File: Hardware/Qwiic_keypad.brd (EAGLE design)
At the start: 25.4 x 25.4 mm, 36 parts, among them J3 PTH, J6 AVR_SPI_PROG_3X2TESTPOINTS, U3 ATTINY84

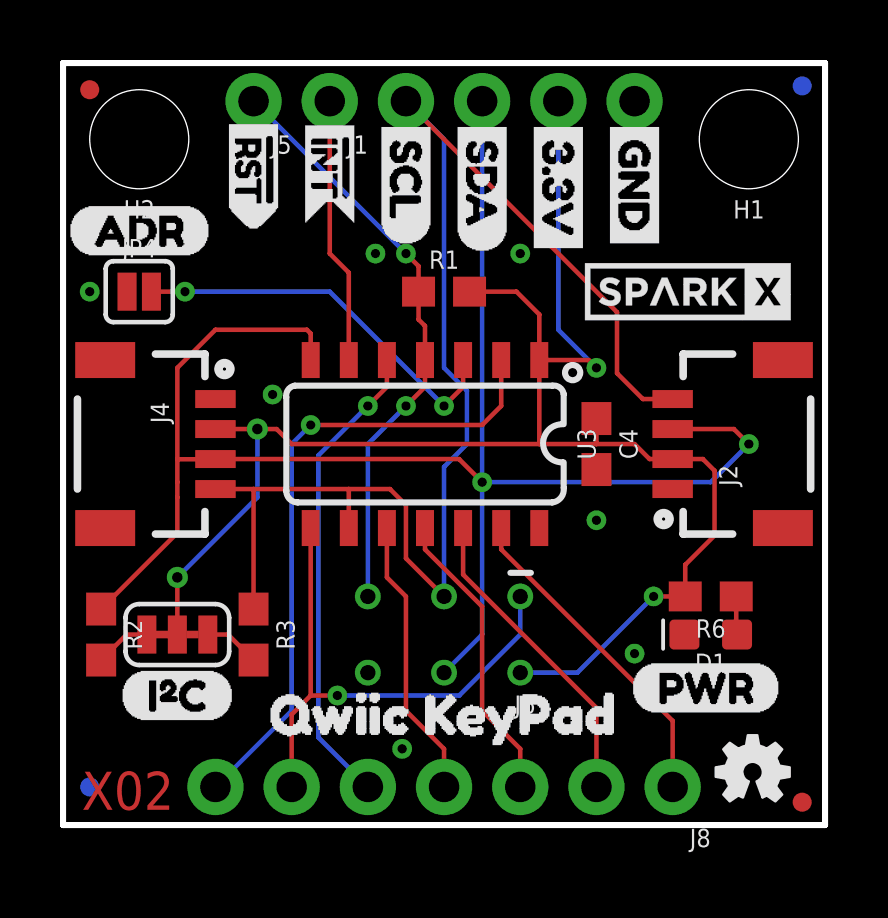
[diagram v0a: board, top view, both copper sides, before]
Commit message: updating hardware
-SFE logo in schematic (w/ slight re-arrange to fit)

-changed version in sch (and brd) to v10

-bumped traces up from 6 mils to 8 mils.

-bumped vias up from 12 mils to 15 mils.

-switched to "sfe tight" drc

-minor trace nudgeing to avoid clearance warnings.

-increased "pass through" 3.3V trace to 16 mils. added more GND vias.
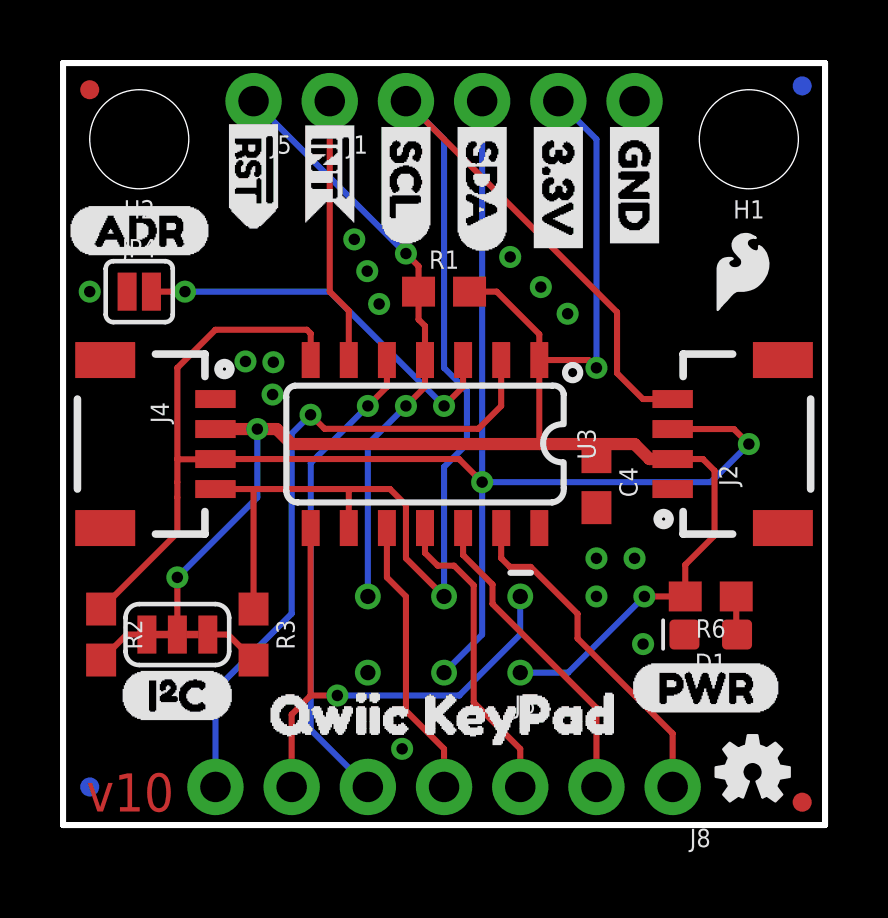
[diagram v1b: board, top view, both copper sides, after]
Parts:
- removed U$1, U$2: SPARKX-LOGO3, SparkX:SPARKX-SMALL
- added LOGO3: SFE_LOGO_FLAME.1_INCH, SparkFun-Aesthetics:SFE_LOGO_FLAME_.1
- moved C4 1.27 mm to (17.8, 11.4)
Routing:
- net 3.3V: track 55.6 -> 54.7 mm
- net 7: track 21.5 -> 22.1 mm
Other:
- board text added: "Revised by: Pete Lewis"
- board text added: "v10"
- board text removed: "X02"

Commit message: Locking footprint on 1x7 connector to keypad
This will help with holding position during selective solder
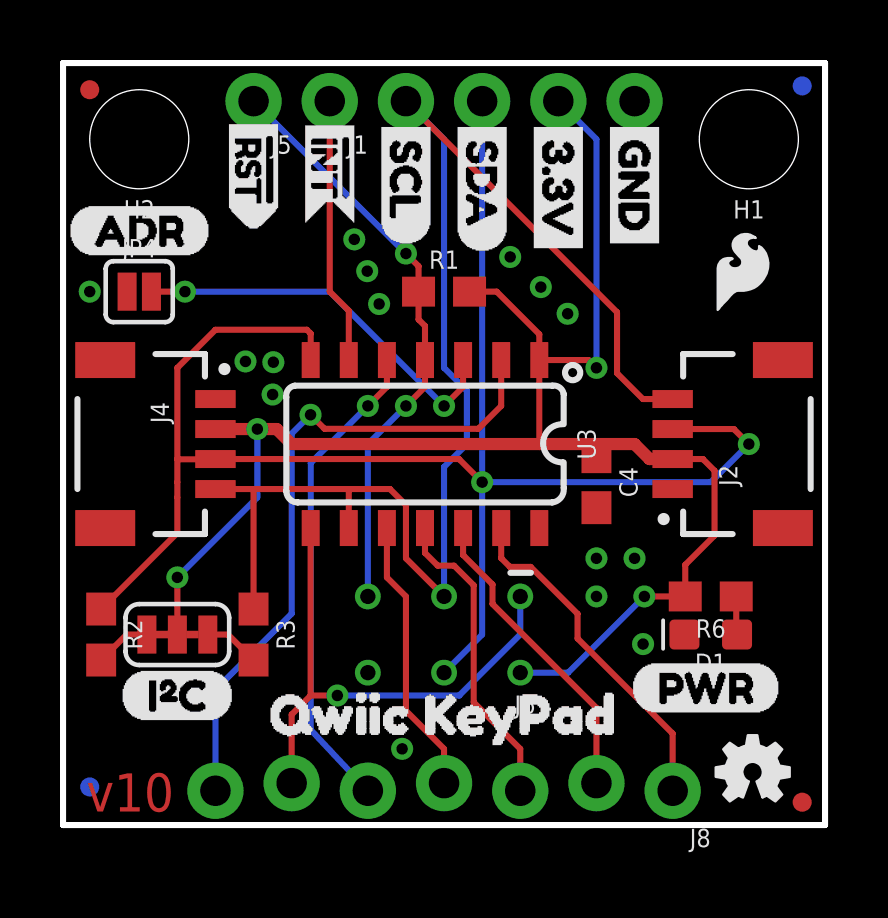
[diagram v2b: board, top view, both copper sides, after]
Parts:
- J2, J4: device SparkFun-Connectors:1X04_1MM_RA -> SparkFun-Connectors:JST04_1MM_RA
- J8: device SparkFun-Connectors:1X07_NO_SILK -> SparkFun-Connectors:1X07_LOCK_NO_SILK
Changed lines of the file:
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@@
 <?xml version="1.0" encoding="utf-8"?>
 <!DOCTYPE eagle SYSTEM "eagle.dtd">
-<eagle version="6.5.0">
+<eagle version="9.2.2">
 <drawing>
 <settings>
-<setting alwaysvectorfont="yes"/>
+<setting alwaysvectorfont="no"/>
+<setting keepoldvectorfont="yes"/>
 <setting verticaltext="up"/>
 </settings>
@@
 <param name="dpMaxLengthDifference" value="10mm"/>
 <param name="dpGapFactor" value="2.5"/>
-<param name="checkGrid" value="0"/>
 <param name="checkAngle" value="1"/>
 <param name="checkFont" value="1"/>
 <param name="checkRestrict" value="1"/>
+<param name="checkStop" value="0"/>
+<param name="checkValues" value="0"/>
+<param name="checkNames" value="1"/>
+<param name="checkWireStubs" value="1"/>
+<param name="checkPolygonWidth" value="0"/>
 <param name="useDiameter" value="13"/>
 <param name="maxErrors" value="50"/>
@@
 <pass name="Default">
 <param name="RoutingGrid" value="50mil"/>
+<param name="AutoGrid" value="1"/>
+<param name="Efforts" value="0"/>
+<param name="TopRouterVariant" value="1"/>
 <param name="tpViaShape" value="round"/>
 <param name="PrefDir.1" value="|"/>
@@
 <element name="JP2" library="SparkFun" package="MICRO-FIDUCIAL" value="FIDUCIALUFIDUCIAL" x="0.889" y="24.511" smashed="yes" rot="R180"/>
 <element name="JP6" library="SparkFun" package="MICRO-FIDUCIAL" value="FIDUCIALUFIDUCIAL" x="24.638" y="0.762" smashed="yes" rot="R180"/>
-<element name="J2" library="SparkFun-Connectors" package="1X04_1MM_RA" value="" x="20.32" y="12.7" smashed="yes" rot="R90">
+<element name="J2" library="SparkFun-Connectors" package="JST04_1MM_RA" value="" x="20.32" y="12.7" smashed="yes" rot="R90">
 <attribute name="NAME" x="22.479" y="11.303" size="0.6096" layer="25" font="vector" ratio="20" rot="R90"/>
 <attribute name="PROD_ID" value="CONN-13694" x="20.32" y="12.7" size="1.778" layer="27" rot="R90" display="off"/>
@@
 <attribute name="VALUE" x="17.018" y="11.43" size="0.6096" layer="27" font="vector" ratio="20" rot="R270" align="top-center"/>
 </element>
-<element name="J4" library="SparkFun-Connectors" package="1X04_1MM_RA" value="" x="5.08" y="12.7" smashed="yes" rot="R270">
+<element name="J4" library="SparkFun-Connectors" package="JST04_1MM_RA" value="" x="5.08" y="12.7" smashed="yes" rot="R270">
 <attribute name="NAME" x="2.921" y="14.097" size="0.6096" layer="25" font="vector" ratio="20" rot="R270"/>
 <attribute name="PROD_ID" value="CONN-13694" x="5.08" y="12.7" size="1.778" layer="27" rot="R270" display="off"/>
@@
 <attribute name="VALUE" x="2.54" y="24.892" size="0.6096" layer="27" font="vector" ratio="20" rot="R180" align="top-center"/>
 </element>
-<element name="J8" library="SparkFun-Connectors" package="1X07_NO_SILK" value="" x="20.32" y="1.27" smashed="yes" rot="R180">
+<element name="J8" library="SparkFun-Connectors" package="1X07_LOCK_NO_SILK" value="" x="20.32" y="1.27" smashed="yes" rot="R180">
 <attribute name="NAME" x="21.59" y="-0.127" size="0.6096" layer="25" font="vector" ratio="20" rot="R180"/>
 <attribute name="VALUE" x="21.59" y="3.302" size="0.6096" layer="27" font="vector" ratio="20" rot="R180"/>
@@
 </element>
 <element name="U$12" library="buzzard_labels (12)" package="#INT1" value="" x="8.89" y="24.003" smashed="yes" rot="R270"/>
-<element name="LOGO3" library="SparkFun-Aesthetics" package="SFE_LOGO_FLAME_.1" value="SFE_LOGO_FLAME.1_INCH" x="22.6441" y="18.46071875"/>
+<element name="LOGO3" library="SparkFun-Aesthetics" package="SFE_LOGO_FLAME_.1" value="SFE_LOGO_FLAME.1_INCH" x="22.6441" y="18.46071875" smashed="yes"/>
 </elements>
 <signals>
@@
 <wire x1="11.43" y1="7.62" x2="11.43" y2="3.81" width="0.2032" layer="1"/>
 <wire x1="11.43" y1="3.81" x2="12.7" y2="2.54" width="0.2032" layer="1"/>
-<wire x1="12.7" y1="2.54" x2="12.7" y2="1.27" width="0.2032" layer="1"/>
+<wire x1="12.7" y1="2.54" x2="12.7" y2="1.397" width="0.2032" layer="1"/>
 <wire x1="10.795" y1="9.9" x2="10.795" y2="8.255" width="0.2032" layer="1"/>
 <wire x1="10.795" y1="8.255" x2="11.43" y2="7.62" width="0.2032" layer="1"/>
@@
 <contactref element="J8" pad="3"/>
 <wire x1="13.688059375" y1="4.091940625" x2="15.24" y2="2.54" width="0.2032" layer="1"/>
-<wire x1="15.24" y1="2.54" x2="15.24" y2="1.27" width="0.2032" layer="1"/>
+<wire x1="15.24" y1="2.54" x2="15.24" y2="1.143" width="0.2032" layer="1"/>
 <wire x1="12.065" y1="9.070340625" x2="12.065" y2="9.9" width="0.2032" layer="1"/>
 <wire x1="13.688059375" y1="4.091940625" x2="13.688059375" y2="7.99338125" width="0.2032" layer="1"/>
@@
 <contactref element="U3" pad="12"/>
 <contactref element="J8" pad="2"/>
-<wire x1="17.78" y1="3.90500625" x2="17.78" y2="1.27" width="0.2032" layer="1"/>
+<wire x1="17.78" y1="3.90500625" x2="17.78" y2="1.397" width="0.2032" layer="1"/>
 <wire x1="13.335" y1="9.9" x2="13.335" y2="8.999221875" width="0.2032" layer="1"/>
 <wire x1="14.315440625" y1="7.369565625" x2="17.78" y2="3.90500625" width="0.2032" layer="1"/>
@@
 <wire x1="15.58544375" y1="8.60551875" x2="14.894559375" y2="8.60551875" width="0.2032" layer="1"/>
 <wire x1="14.894559375" y1="8.60551875" x2="14.605" y2="8.895078125" width="0.2032" layer="1"/>
-<wire x1="20.32" y1="1.27" x2="20.32" y2="3.050540625" width="0.2032" layer="1"/>
+<wire x1="20.32" y1="1.143" x2="20.32" y2="3.050540625" width="0.2032" layer="1"/>
 <wire x1="20.32" y1="3.050540625" x2="17.15008125" y2="6.220459375" width="0.2032" layer="1"/>
 </signal>
@@
 <wire x1="15.24" y1="6.35" x2="15.24" y2="7.62" width="0.2032" layer="16"/>
 <via x="9.144" y="4.318" extent="1-16" drill="0.381"/>
-<wire x1="7.62" y1="1.27" x2="7.62" y2="3.683" width="0.2032" layer="1"/>
+<wire x1="7.62" y1="1.397" x2="7.62" y2="3.683" width="0.2032" layer="1"/>
 <wire x1="7.62" y1="3.683" x2="8.255" y2="4.318" width="0.2032" layer="1"/>
 <wire x1="8.255" y1="4.318" x2="9.144" y2="4.318" width="0.2032" layer="1"/>
@@
 <wire x1="7.62" y1="7.04341875" x2="7.62" y2="13.0454375" width="0.2032" layer="16"/>
 <wire x1="13.843" y1="13.208" x2="8.71728125" y2="13.208" width="0.2032" layer="1"/>
-<wire x1="5.08" y1="1.27" x2="5.08" y2="4.50341875" width="0.2032" layer="16"/>
+<wire x1="5.08" y1="1.143" x2="5.08" y2="4.50341875" width="0.2032" layer="16"/>
 <wire x1="5.08" y1="4.50341875" x2="7.62" y2="7.04341875" width="0.2032" layer="16"/>
 <wire x1="7.62" y1="13.0454375" x2="8.249921875" y2="13.675359375" width="0.2032" layer="16"/>
@@
 <wire x1="8.509" y1="12.319" x2="8.89" y2="12.7" width="0.2032" layer="16"/>
 <wire x1="8.89" y1="12.7" x2="10.16" y2="13.97" width="0.2032" layer="16"/>
-<wire x1="10.16" y1="1.27" x2="8.257540625" y2="3.172459375" width="0.2032" layer="16"/>
+<wire x1="10.16" y1="1.143" x2="8.257540625" y2="3.172459375" width="0.2032" layer="16"/>
 <wire x1="8.257540625" y1="3.172459375" x2="8.257540625" y2="12.067540625" width="0.2032" layer="16"/>
 <wire x1="8.257540625" y1="12.067540625" x2="8.509" y2="12.319" width="0.2032" layer="16"/>
@@
 </signal>
 </signals>
+<mfgpreviewcolors>
+<mfgpreviewcolor name="soldermaskcolor" color="0xC8008000"/>
+<mfgpreviewcolor name="silkscreencolor" color="0xFFFEFEFE"/>
+<mfgpreviewcolor name="backgroundcolor" color="0xFF282828"/>
+<mfgpreviewcolor name="coppercolor" color="0xFFFFBF00"/>
+<mfgpreviewcolor name="substratecolor" color="0xFF786E46"/>
+</mfgpreviewcolors>
 <errors>
 </errors>

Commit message: added INT pullup resistor
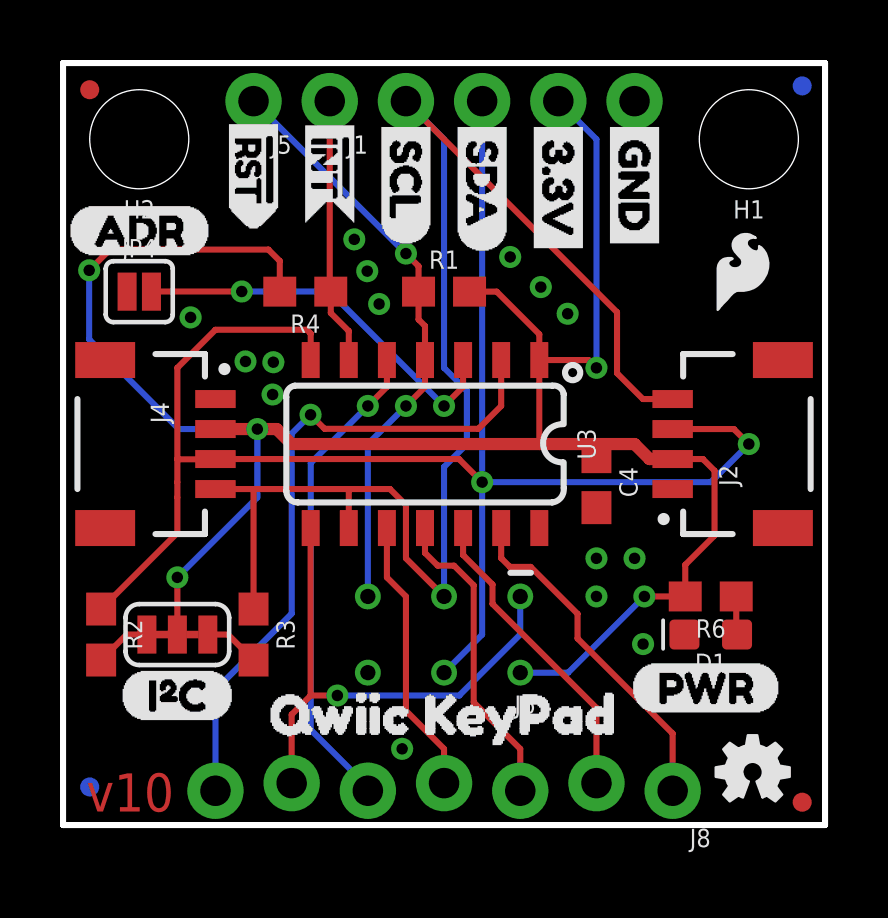
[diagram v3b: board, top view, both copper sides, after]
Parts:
- added R4: 4.7k, SparkFun-Resistors:0603
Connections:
- net !INT: now also R4.1
- net 3.3V: now also R4.2
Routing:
- net 3.3V: track 54.7 -> 71.7 mm, vias 4 -> 5
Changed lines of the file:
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@@
 <layer number="29" name="tStop" color="7" fill="3" visible="no" active="yes"/>
 <layer number="30" name="bStop" color="7" fill="6" visible="no" active="yes"/>
-<layer number="31" name="tCream" color="7" fill="4" visible="no" active="yes"/>
+<layer number="31" name="tCream" color="7" fill="4" visible="yes" active="yes"/>
 <layer number="32" name="bCream" color="7" fill="5" visible="no" active="yes"/>
 <layer number="33" name="tFinish" color="6" fill="3" visible="no" active="yes"/>
@@
 <element name="U$12" library="buzzard_labels (12)" package="#INT1" value="" x="8.89" y="24.003" smashed="yes" rot="R270"/>
 <element name="LOGO3" library="SparkFun-Aesthetics" package="SFE_LOGO_FLAME_.1" value="SFE_LOGO_FLAME.1_INCH" x="22.6441" y="18.46071875" smashed="yes"/>
+<element name="R4" library="SparkFun-Resistors" package="0603" value="4.7k" x="8.0746625" y="17.78" smashed="yes" rot="R180">
+<attribute name="NAME" x="8.0746625" y="17.018" size="0.6096" layer="25" font="vector" ratio="20" rot="R180" align="bottom-center"/>
+<attribute name="PROD_ID" value="RES-07857" x="8.0746625" y="17.78" size="1.778" layer="27" rot="R180" display="off"/>
+<attribute name="VALUE" x="8.0746625" y="18.542" size="0.6096" layer="27" font="vector" ratio="20" rot="R180" align="top-center"/>
+</element>
 </elements>
 <signals>
@@
 <wire x1="17.78" y1="15.24" x2="17.78" y2="22.86" width="0.2032" layer="16"/>
 <wire x1="17.78" y1="22.86" x2="16.51" y2="24.13" width="0.2032" layer="16"/>
+<contactref element="R4" pad="2"/>
+<via x="0.871221875" y="18.4912" extent="1-16" drill="0.381"/>
+<wire x1="6.477" y1="13.2" x2="3.8561" y2="13.2" width="0.2032" layer="16"/>
+<wire x1="0.871221875" y1="18.4912" x2="1.562103125" y2="19.18208125" width="0.2032" layer="1"/>
+<wire x1="0.871221875" y1="16.184878125" x2="0.871221875" y2="18.4912" width="0.2032" layer="16"/>
+<wire x1="3.8561" y1="13.2" x2="0.871221875" y2="16.184878125" width="0.2032" layer="16"/>
+<wire x1="7.2246625" y1="18.80271875" x2="7.2246625" y2="17.78" width="0.2032" layer="1"/>
+<wire x1="1.562103125" y1="19.18208125" x2="6.8453" y2="19.18208125" width="0.2032" layer="1"/>
+<wire x1="6.8453" y1="19.18208125" x2="7.2246625" y2="18.80271875" width="0.2032" layer="1"/>
 </signal>
 <signal name="GND">
@@
 <via x="17.78" y="8.89" extent="1-16" drill="0.381"/>
 <via x="11.303" y="2.54" extent="1-16" drill="0.381"/>
-<via x="0.889" y="17.78" extent="1-16" drill="0.381"/>
+<via x="4.251959375" y="16.921478125" extent="1-16" drill="0.381"/>
 <via x="6.985" y="14.351" extent="1-16" drill="0.381"/>
 <via x="9.707878125" y="19.5224375" extent="1-16" drill="0.381"/>
@@
 <contactref element="J1" pad="1"/>
 <contactref element="U3" pad="6"/>
-<wire x1="9.525" y1="15.5" x2="9.525" y2="17.145" width="0.2032" layer="1"/>
-<wire x1="9.525" y1="17.145" x2="8.89" y2="17.78" width="0.2032" layer="1"/>
-<wire x1="8.89" y1="17.78" x2="8.89" y2="24.13" width="0.2032" layer="1"/>
+<contactref element="R4" pad="1"/>
+<wire x1="9.525" y1="15.5" x2="9.525" y2="16.46681875" width="0.2032" layer="1"/>
+<wire x1="9.525" y1="16.46681875" x2="8.9246625" y2="17.06715625" width="0.2032" layer="1"/>
+<wire x1="8.9246625" y1="17.06715625" x2="8.9246625" y2="17.78" width="0.2032" layer="1"/>
+<wire x1="8.9246625" y1="17.78" x2="8.89" y2="17.8146625" width="0.2032" layer="1"/>
+<wire x1="8.89" y1="17.8146625" x2="8.89" y2="24.13" width="0.2032" layer="1"/>
 </signal>
 <signal name="ADD1">
 <contactref element="U3" pad="3"/>
 <contactref element="JP4" pad="2"/>
-<wire x1="2.9464" y1="17.78" x2="4.064" y2="17.78" width="0.2032" layer="1"/>
-<via x="4.064" y="17.78" extent="1-16" drill="0.381"/>
+<wire x1="5.9563" y1="17.78508125" x2="2.95148125" y2="17.78508125" width="0.2032" layer="1"/>
+<wire x1="2.9464" y1="17.78" x2="2.95148125" y2="17.78508125" width="0.2032" layer="1"/>
+<via x="5.9563" y="17.78508125" extent="1-16" drill="0.381"/>
 <via x="12.7" y="13.97" extent="1-16" drill="0.381"/>
 <wire x1="13.335" y1="15.5" x2="13.335" y2="14.605" width="0.2032" layer="1"/>
 <wire x1="13.335" y1="14.605" x2="12.7" y2="13.97" width="0.2032" layer="1"/>
-<wire x1="12.7" y1="13.97" x2="8.89" y2="17.78" width="0.2032" layer="16"/>
-<wire x1="8.89" y1="17.78" x2="4.064" y2="17.78" width="0.2032" layer="16"/>
+<wire x1="12.7" y1="13.97" x2="8.88491875" y2="17.78508125" width="0.2032" layer="16"/>
+<wire x1="8.88491875" y1="17.78508125" x2="5.9563" y2="17.78508125" width="0.2032" layer="16"/>
 </signal>
 <signal name="4">
@@
 <wire x1="10.795" y1="14.605" x2="10.16" y2="13.97" width="0.2032" layer="1"/>
 <via x="10.16" y="13.97" extent="1-16" drill="0.381"/>
-<wire x1="8.509" y1="12.319" x2="8.89" y2="12.7" width="0.2032" layer="16"/>
-<wire x1="8.89" y1="12.7" x2="10.16" y2="13.97" width="0.2032" layer="16"/>
-<wire x1="10.16" y1="1.143" x2="8.257540625" y2="3.172459375" width="0.2032" layer="16"/>
-<wire x1="8.257540625" y1="3.172459375" x2="8.257540625" y2="12.067540625" width="0.2032" layer="16"/>
-<wire x1="8.257540625" y1="12.067540625" x2="8.509" y2="12.319" width="0.2032" layer="16"/>
+<wire x1="8.257540625" y1="12.067540625" x2="10.16" y2="13.97" width="0.2032" layer="16"/>
+<wire x1="8.257540625" y1="12.067540625" x2="8.257540625" y2="3.172459375" width="0.2032" layer="16"/>
+<wire x1="8.257540625" y1="3.172459375" x2="10.16" y2="1.27" width="0.2032" layer="16"/>
+<wire x1="10.16" y1="1.27" x2="10.16" y2="1.143" width="0.2032" layer="16"/>
 </signal>
 <signal name="SCL">
